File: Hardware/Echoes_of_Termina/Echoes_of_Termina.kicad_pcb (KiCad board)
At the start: 2 copper layers, 99 x 59.5 mm, 81 parts, among them J1 USB_C_Receptacle_USB2.0_8P, J2 Conn_01x03_Socket, J3 Conn_01x02_Socket, J4 Conn_01x02_Socket, Q1 PMOS, Q2 2N7002K, Q3 PMOS, U1 TP4056, U2 AP2112K-3.3, U3 ESP32-WROOM-32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

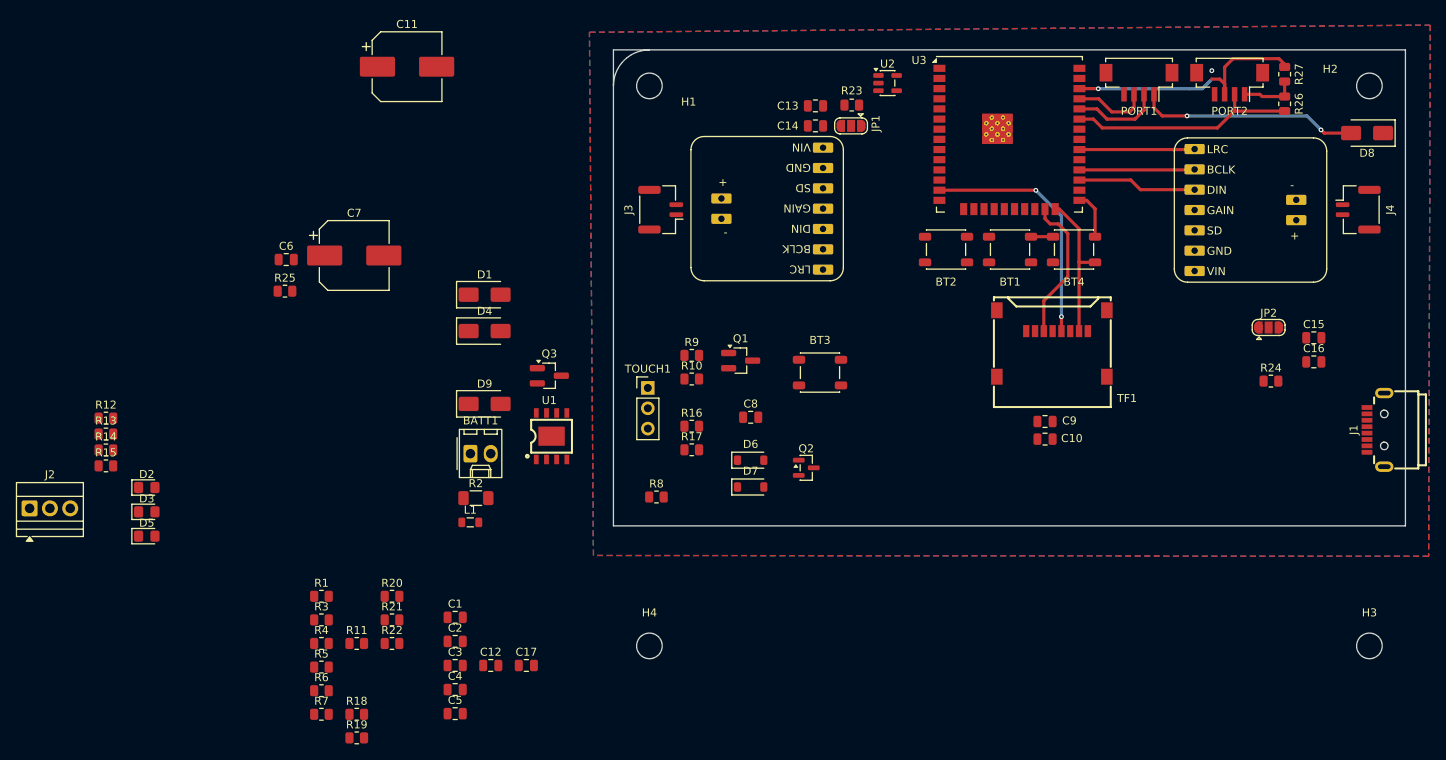
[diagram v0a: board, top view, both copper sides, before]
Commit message: Echoes layout for revision before fabrication
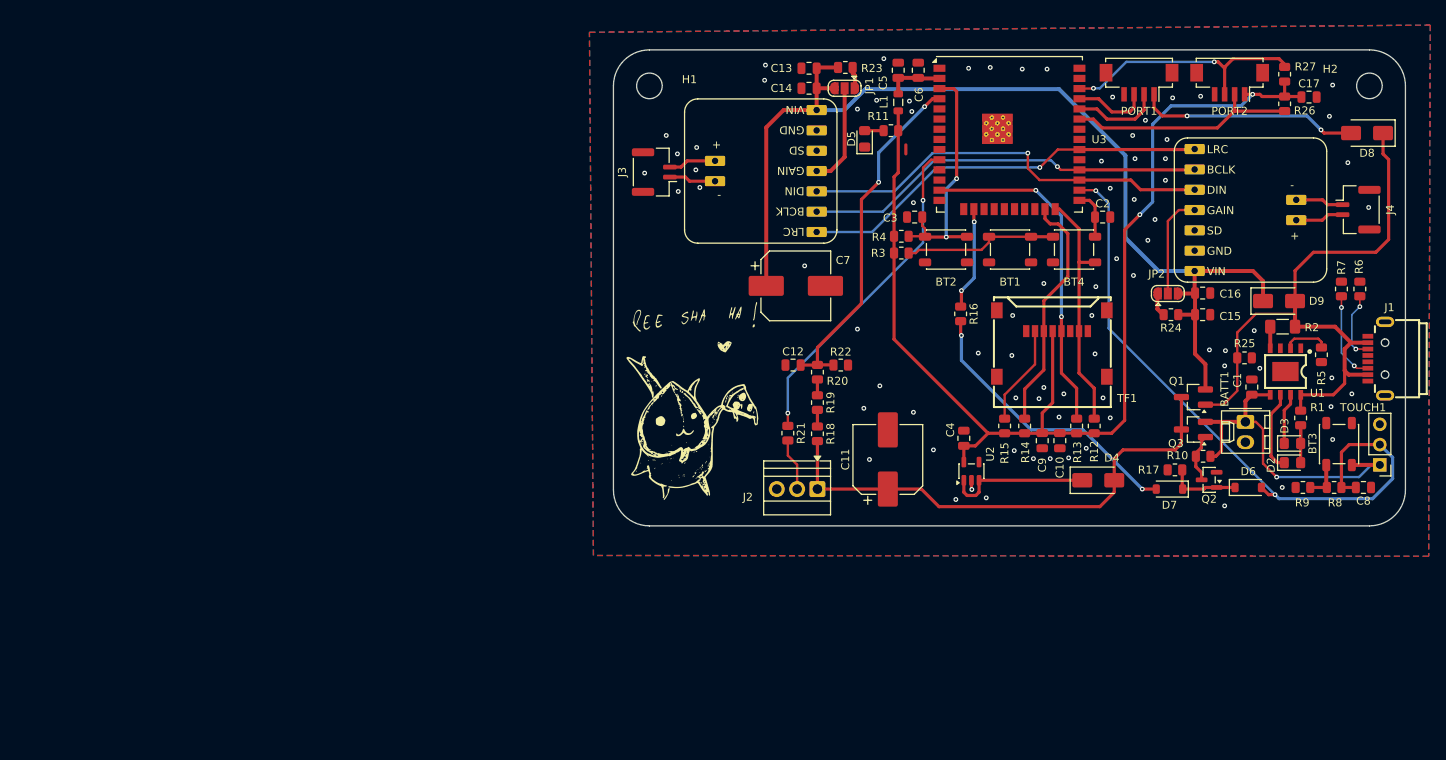
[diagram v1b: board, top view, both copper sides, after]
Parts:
- removed D1: SS14, Diode_SMD:D_SMA
- removed H3, H4: MountingHole, MountingHole:MountingHole_3.2mm_M3
- moved D3 143.5 mm to (215.3, 118.3)
- moved D2 143.2 mm to (215.3, 120.7)
- moved R6 139.2 mm to (223.7, 99.0), turned to -90 degrees
- moved R7 138.1 mm to (221.4, 99.0), turned to -90 degrees
- moved R5 131.0 mm to (218.9, 107.2), turned to 90 degrees
- moved R1 124.4 mm to (216.3, 115.1), turned to -90 degrees
- moved R12 123.5 mm to (190.5, 116.1), turned to 90 degrees
- moved R13 121.3 mm to (188.3, 116.1), turned to 90 degrees
- moved C17 120.9 mm to (217.3, 75.0)
- moved R25 120.2 mm to (209.3, 107.6), turned to 180 degrees
- moved R14 114.9 mm to (181.8, 116.1), turned to 90 degrees
- moved R15 112.5 mm to (179.3, 116.1), turned to 90 degrees
- moved C1 103.7 mm to (210.2, 111.3), turned to 90 degrees
- moved R2 103.1 mm to (214.1, 103.7), turned to 180 degrees
- moved D5 102.6 mm to (161.8, 80.2), turned to 90 degrees
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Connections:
- C7 pad 1: Net-(D1-K) -> V_SPK
- D4 pad 1: Net-(D1-K) -> Net-(D4-K)
- U2 pad 1: Net-(D1-K) -> Net-(D4-K)
- U2 pad 3: Net-(D1-K) -> Net-(D4-K)
- U3 pad 10: latch_enable -> Strip_out
- U3 pad 11: Button_GPIO -> unconnected-(U3-IO26-Pad11)
- U3 pad 16: Strip_out -> latch_enable
- U3 pad 26: unconnected-(U3-IO4-Pad26) -> Button_GPIO
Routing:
- net +3.3V: track 6.99 -> 143.8 mm, vias 0 -> 2
- net V_SPK: track 0.00 -> 132.1 mm
- net Button_GPIO: track 0.00 -> 83.7 mm, vias 0 -> 2
- net +5V: track 0.00 -> 80.6 mm
- net V_REG: track 0.00 -> 63.9 mm
- net ADC1_0: track 0.00 -> 44.2 mm, vias 0 -> 2
- net +BATT: track 0.00 -> 42.6 mm, vias 0 -> 1
- net Strip_out: track 0.00 -> 41.7 mm, vias 0 -> 2
- net I2S_DOUT: track 14.9 -> 52.2 mm, vias 0 -> 1
- net I2S_LRC: track 14.4 -> 51.5 mm, vias 0 -> 1
- net I2S_BCLK: track 14.4 -> 50.4 mm, vias 0 -> 1
- net Net-(D7-A): track 0.00 -> 35.9 mm, vias 0 -> 2
- net EN: track 0.00 -> 31.0 mm, vias 0 -> 2
- net Net-(D4-K): track 0.00 -> 18.1 mm
- net PROG: track 8.63 -> 25.4 mm
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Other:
- outline, holes or cut-outs redrawn
